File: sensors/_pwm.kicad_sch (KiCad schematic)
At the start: 21 parts, among them U2 PCA9685PW, Y2 ASE-xxxMHz

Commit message: add Vref
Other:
- title: (none) -> PilotPi: Sensors
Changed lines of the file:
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@@
 	(generator_version "10.0")
 	(paper "A4")
+	(title_block
+		(title "PilotPi: Sensors")
+		(date "15 nov 2012")
+		(rev "4")
+	)
 	(junction
 		(at 184.15 80.01)

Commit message: added JP_VOLTS, Vref select jumper; VBAT_ADC Jumper
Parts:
- C4, C5: Part (none) -> CC0402X7R50V104KN
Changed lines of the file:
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@@
 			)
 		)
-		(property "Part" ""
+		(property "Part" "CC0402X7R50V104KN"
 			(at 30.48 92.71 0)
 			(hide yes)
@@
 			)
 		)
-		(property "Part" ""
+		(property "Part" "CC0402X7R50V104KN"
 			(at 256.54 92.71 0)
 			(hide yes)

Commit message: use CLK out from CAN controller for UART (use 16 MHz instead of 14.7456MHz); minor changes
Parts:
- C4, C5: value 100nF (104) 10% 16V -> 100nF 10% 16V
- R12: value 3.3KΩ (3301) ±1% -> 3.3KΩ ±1%
- R13, R14, R15, R16, R17, R18, R19, R20, R21, R22, R23, R24, R25, R26, R27, R28: value 220Ω (2200) ±1% -> 220Ω ±1%
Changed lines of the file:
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@@
 			)
 		)
-		(property "Value" "220Ω (2200) ±1%"
+		(property "Value" "220Ω ±1%"
 			(at 129.032 96.774 90)
 			(show_name no)
@@
 			)
 		)
-		(property "Value" "220Ω (2200) ±1%"
+		(property "Value" "220Ω ±1%"
 			(at 104.902 89.154 90)
 			(show_name no)
@@
 			)
 		)
-		(property "Value" "220Ω (2200) ±1%"
+		(property "Value" "220Ω ±1%"
 			(at 104.902 78.994 90)
 			(show_name no)
@@
 			)
 		)
-		(property "Value" "220Ω (2200) ±1%"
+		(property "Value" "220Ω ±1%"
 			(at 129.032 81.534 90)
 			(show_name no)
@@
 			)
 		)
-		(property "Value" "220Ω (2200) ±1%"
+		(property "Value" "220Ω ±1%"
 			(at 104.902 73.914 90)
 			(show_name no)
@@
 			)
 		)
-		(property "Value" "220Ω (2200) ±1%"
+		(property "Value" "220Ω ±1%"
 			(at 104.902 94.234 90)
 			(show_name no)
@@
 			)
 		)
-		(property "Value" "220Ω (2200) ±1%"
+		(property "Value" "220Ω ±1%"
 			(at 129.032 112.014 90)
 			(show_name no)
@@
 			)
 		)
-		(property "Value" "220Ω (2200) ±1%"
+		(property "Value" "220Ω ±1%"
 			(at 104.902 109.474 90)
 			(show_name no)
@@
 			)
 		)
-		(property "Value" "220Ω (2200) ±1%"
+		(property "Value" "220Ω ±1%"
 			(at 104.902 99.314 90)
 			(show_name no)
@@
 			)
 		)
-		(property "Value" "220Ω (2200) ±1%"
+		(property "Value" "220Ω ±1%"
 			(at 129.032 91.694 90)
 			(show_name no)
@@
 			)
 		)
-		(property "Value" "220Ω (2200) ±1%"
+		(property "Value" "220Ω ±1%"
 			(at 129.032 106.934 90)
 			(show_name no)
@@
 			)
 		)
-		(property "Value" "220Ω (2200) ±1%"
+		(property "Value" "220Ω ±1%"
 			(at 129.032 101.854 90)
 			(show_name no)
@@
 			)
 		)
-		(property "Value" "100nF (104) 10% 16V"
+		(property "Value" "100nF 10% 16V"
 			(at 25.146 101.092 90)
 			(show_name no)
@@
 			)
 		)
-		(property "Value" "220Ω (2200) ±1%"
+		(property "Value" "220Ω ±1%"
 			(at 129.032 76.454 90)
 			(show_name no)
@@
 			)
 		)
-		(property "Value" "100nF (104) 10% 16V"
+		(property "Value" "100nF 10% 16V"
 			(at 262.89 98.806 90)
 			(show_name no)
@@
 			)
 		)
-		(property "Value" "220Ω (2200) ±1%"
+		(property "Value" "220Ω ±1%"
 			(at 104.902 104.394 90)
 			(show_name no)
@@
 			)
 		)
-		(property "Value" "220Ω (2200) ±1%"
+		(property "Value" "220Ω ±1%"
 			(at 104.902 84.074 90)
 			(show_name no)
@@
 			)
 		)
-		(property "Value" "3.3KΩ (3301) ±1%"
+		(property "Value" "3.3KΩ ±1%"
 			(at 188.468 92.964 90)
 			(show_name no)
@@
 			)
 		)
-		(property "Value" "220Ω (2200) ±1%"
+		(property "Value" "220Ω ±1%"
 			(at 129.032 86.614 90)
 			(show_name no)

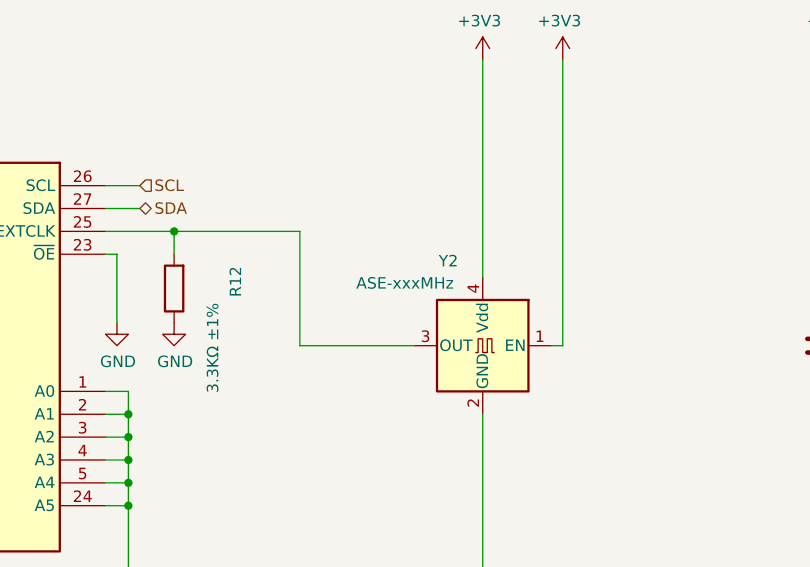
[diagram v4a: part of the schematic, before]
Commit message: use 2x8 for ADC header; added part numbers
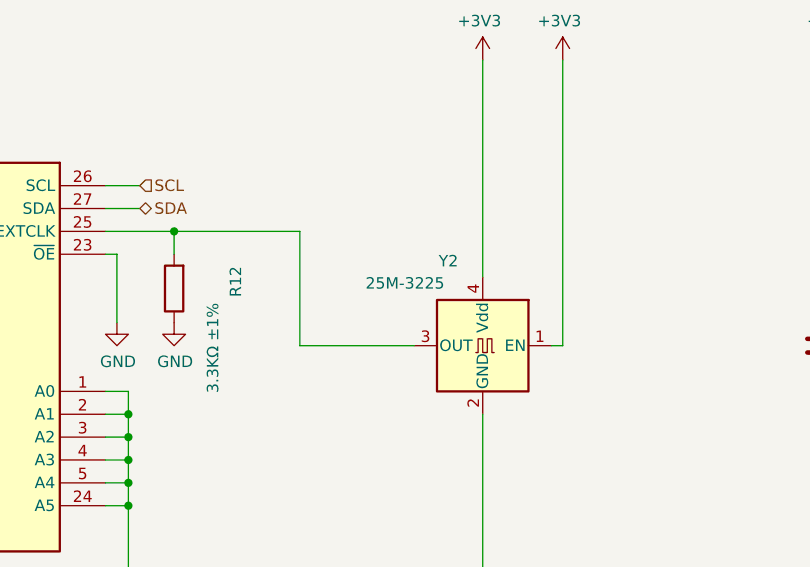
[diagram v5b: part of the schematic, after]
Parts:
- R12: Part (none) -> 0402WGF3301TCE
- R13, R14, R15, R16, R17, R18, R19, R20, R21, R22, R23, R24, R25, R26, R27, R28: Part (none) -> RC0402FR-07220RL
- U2: Part (none) -> PCA9685PW/Q900,118
- Y2: value ASE-xxxMHz -> 25M-3225; Part (none) -> Y322525MNCCZ
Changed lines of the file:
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@@
 			)
 		)
-		(property "Part" ""
+		(property "Part" "RC0402FR-07220RL"
 			(at 116.84 97.79 0)
 			(hide yes)
@@
 			)
 		)
-		(property "Part" ""
+		(property "Part" "RC0402FR-07220RL"
 			(at 92.71 90.17 0)
 			(hide yes)
@@
 			)
 		)
-		(property "Part" ""
+		(property "Part" "RC0402FR-07220RL"
 			(at 92.71 80.01 0)
 			(hide yes)
@@
 			)
 		)
-		(property "Part" ""
+		(property "Part" "RC0402FR-07220RL"
 			(at 116.84 82.55 0)
 			(hide yes)
@@
 			)
 		)
-		(property "Part" ""
+		(property "Part" "RC0402FR-07220RL"
 			(at 92.71 74.93 0)
 			(hide yes)
@@
 			)
 		)
-		(property "Part" ""
+		(property "Part" "RC0402FR-07220RL"
 			(at 92.71 95.25 0)
 			(hide yes)
@@
 			)
 		)
-		(property "Part" ""
+		(property "Part" "RC0402FR-07220RL"
 			(at 116.84 113.03 0)
 			(hide yes)
@@
 			)
 		)
-		(property "Part" ""
+		(property "Part" "RC0402FR-07220RL"
 			(at 92.71 110.49 0)
 			(hide yes)
@@
 			)
 		)
+		(property "Part" "PCA9685PW/Q900,118"
+			(at 158.75 92.71 0)
+			(hide yes)
+			(show_name no)
+			(do_not_autoplace no)
+			(effects
+				(font
+					(size 1.27 1.27)
+				)
+			)
+		)
 		(pin "10"
 		)
@@
 			)
 		)
-		(property "Part" ""
+		(property "Part" "RC0402FR-07220RL"
 			(at 92.71 100.33 0)
 			(hide yes)
@@
 			)
 		)
-		(property "Part" ""
+		(property "Part" "RC0402FR-07220RL"
 			(at 116.84 92.71 0)
 			(hide yes)
@@
 			)
 		)
-		(property "Part" ""
+		(property "Part" "RC0402FR-07220RL"
 			(at 116.84 107.95 0)
 			(hide yes)
@@
 			)
 		)
-		(property "Part" ""
+		(property "Part" "RC0402FR-07220RL"
 			(at 116.84 102.87 0)
 			(hide yes)
@@
 			)
 		)
-		(property "Part" ""
+		(property "Part" "RC0402FR-07220RL"
 			(at 116.84 77.47 0)
 			(hide yes)
@@
 			)
 		)
-		(property "Part" ""
+		(property "Part" "RC0402FR-07220RL"
 			(at 92.71 105.41 0)
 			(hide yes)
@@
 			)
 		)
-		(property "Part" ""
+		(property "Part" "RC0402FR-07220RL"
 			(at 92.71 85.09 0)
 			(hide yes)
@@
 			)
 		)
-		(property "Part" ""
+		(property "Part" "0402WGF3301TCE"
 			(at 184.15 86.36 0)
 			(hide yes)
@@
 			)
 		)
-		(property "Part" ""
+		(property "Part" "RC0402FR-07220RL"
 			(at 116.84 87.63 0)
 			(hide yes)
@@
 			)
 		)
-		(property "Value" "ASE-xxxMHz"
+		(property "Value" "25M-3225"
 			(at 209.804 85.7818 0)
 			(show_name no)
@@
 			(at 218.44 92.71 0)
 			(hide yes)
+			(show_name no)
+			(do_not_autoplace no)
+			(effects
+				(font
+					(size 1.27 1.27)
+				)
+			)
+		)
+		(property "Part" "Y322525MNCCZ"
+			(at 218.44 92.71 0)
+			(hide yes)

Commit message: replace MS561101 pressure sensor with SPL06-001
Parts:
- C4, C5: Part CC0402X7R50V104KN -> CL05B104KB54PNC
- R13, R14, R15, R16, R17, R18, R19, R20, R21, R22, R23, R24, R25, R26, R27, R28: Part RC0402FR-07220RL -> 0402WGF2200TCE
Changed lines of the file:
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@@
 			)
 		)
-		(property "Part" "RC0402FR-07220RL"
+		(property "Part" "0402WGF2200TCE"
 			(at 116.84 97.79 0)
 			(hide yes)
@@
 			)
 		)
-		(property "Part" "RC0402FR-07220RL"
+		(property "Part" "0402WGF2200TCE"
 			(at 92.71 90.17 0)
 			(hide yes)
@@
 			)
 		)
-		(property "Part" "RC0402FR-07220RL"
+		(property "Part" "0402WGF2200TCE"
 			(at 92.71 80.01 0)
 			(hide yes)
@@
 			)
 		)
-		(property "Part" "RC0402FR-07220RL"
+		(property "Part" "0402WGF2200TCE"
 			(at 116.84 82.55 0)
 			(hide yes)
@@
 			)
 		)
-		(property "Part" "RC0402FR-07220RL"
+		(property "Part" "0402WGF2200TCE"
 			(at 92.71 74.93 0)
 			(hide yes)
@@
 			)
 		)
-		(property "Part" "RC0402FR-07220RL"
+		(property "Part" "0402WGF2200TCE"
 			(at 92.71 95.25 0)
 			(hide yes)
@@
 			)
 		)
-		(property "Part" "RC0402FR-07220RL"
+		(property "Part" "0402WGF2200TCE"
 			(at 116.84 113.03 0)
 			(hide yes)
@@
 			)
 		)
-		(property "Part" "RC0402FR-07220RL"
+		(property "Part" "0402WGF2200TCE"
 			(at 92.71 110.49 0)
 			(hide yes)
@@
 			)
 		)
-		(property "Part" "RC0402FR-07220RL"
+		(property "Part" "0402WGF2200TCE"
 			(at 92.71 100.33 0)
 			(hide yes)
@@
 			)
 		)
-		(property "Part" "RC0402FR-07220RL"
+		(property "Part" "0402WGF2200TCE"
 			(at 116.84 92.71 0)
 			(hide yes)
@@
 			)
 		)
-		(property "Part" "RC0402FR-07220RL"
+		(property "Part" "0402WGF2200TCE"
 			(at 116.84 107.95 0)
 			(hide yes)
@@
 			)
 		)
-		(property "Part" "RC0402FR-07220RL"
+		(property "Part" "0402WGF2200TCE"
 			(at 116.84 102.87 0)
 			(hide yes)
@@
 			)
 		)
-		(property "Part" "CC0402X7R50V104KN"
+		(property "Part" "CL05B104KB54PNC"
 			(at 30.48 92.71 0)
 			(hide yes)
@@
 			)
 		)
-		(property "Part" "RC0402FR-07220RL"
+		(property "Part" "0402WGF2200TCE"
 			(at 116.84 77.47 0)
 			(hide yes)
@@
 			)
 		)
-		(property "Part" "CC0402X7R50V104KN"
+		(property "Part" "CL05B104KB54PNC"
 			(at 256.54 92.71 0)
 			(hide yes)
@@
 			)
 		)
-		(property "Part" "RC0402FR-07220RL"
+		(property "Part" "0402WGF2200TCE"
 			(at 92.71 105.41 0)
 			(hide yes)
@@
 			)
 		)
-		(property "Part" "RC0402FR-07220RL"
+		(property "Part" "0402WGF2200TCE"
 			(at 92.71 85.09 0)
 			(hide yes)
@@
 			)
 		)
-		(property "Part" "RC0402FR-07220RL"
+		(property "Part" "0402WGF2200TCE"
 			(at 116.84 87.63 0)
 			(hide yes)

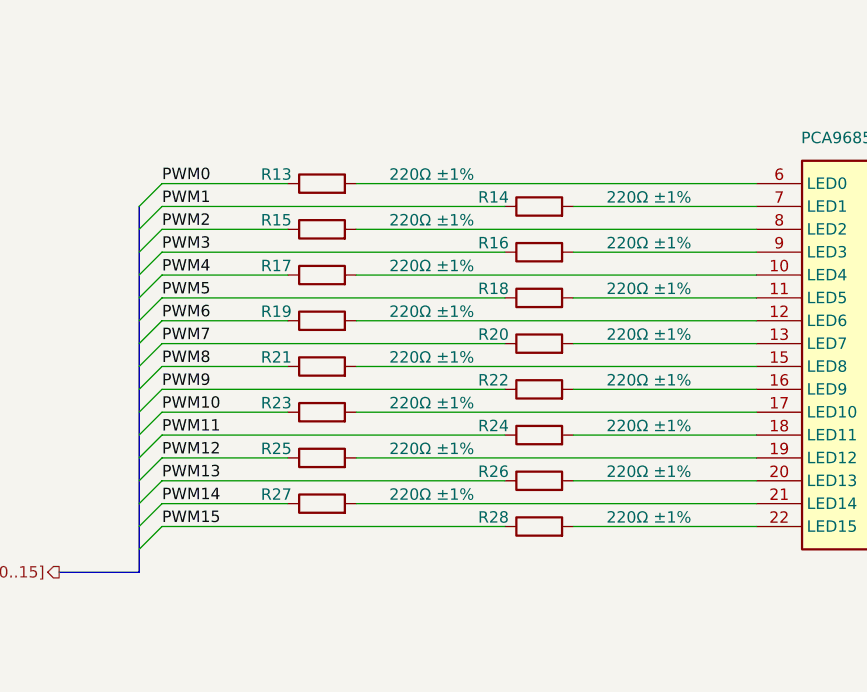
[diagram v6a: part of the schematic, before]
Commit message: move SP3485 to sensors board and connect to UART port A
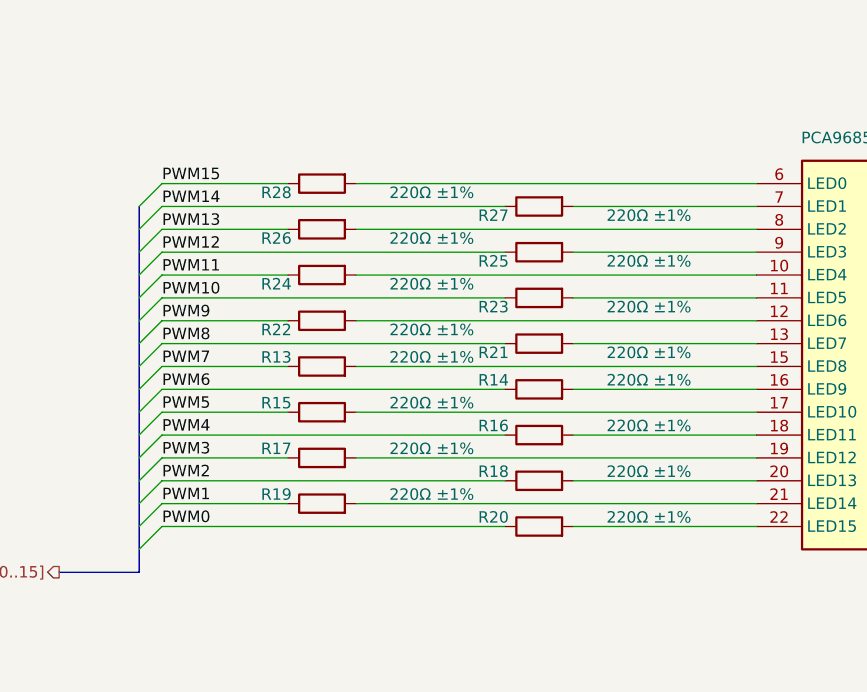
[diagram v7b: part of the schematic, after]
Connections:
- net PWM0: now also R20.1; no longer R13.1
- net PWM1: now also R19.1; no longer R14.1
- net PWM2: now also R18.1; no longer R15.1
- net PWM3: now also R17.1; no longer R16.1
- net PWM4: now also R16.1; no longer R17.1
- net PWM5: now also R15.1; no longer R18.1
- net PWM6: now also R14.1; no longer R19.1
- net PWM7: now also R13.1; no longer R20.1
- net at R22.2: now also U2.12 (LED6); no longer U2.16 (LED9)
- net at R19.2: now also U2.21 (LED14); no longer U2.12 (LED6)
- net at R15.2: now also U2.17 (LED10); no longer U2.8 (LED2)
- net at R16.2: now also U2.18 (LED11); no longer U2.9 (LED3)
- net at R13.2: now also U2.15 (LED8); no longer U2.6 (LED0)
- net at R21.2: now also U2.13 (LED7); no longer U2.15 (LED8)
- net at R28.2: now also U2.6 (LED0); no longer U2.22 (LED15)
- net at R27.2: now also U2.7 (LED1); no longer U2.21 (LED14)
- net at U2.10 (LED4): now also R24.2; no longer R17.2
- net at U2.11 (LED5): now also R23.2; no longer R18.2
- net at R20.2: now also U2.22 (LED15); no longer U2.13 (LED7)
- net at U2.19 (LED12): now also R17.2; no longer R25.2
- net at U2.20 (LED13): now also R18.2; no longer R26.2
- net at R14.2: now also U2.16 (LED9); no longer U2.7 (LED1)
- new net: R26.2, U2.8 (LED2)
- new net: R25.2, U2.9 (LED3)
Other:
- moved on the sheet: R13, R14, R15, R16, R17, R18, R19, R20, R21, R22, R23, R24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

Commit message: use series resistor for external clk; add 1uF caps
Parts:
- added C20: 1uF (105) 10% 50V, Capacitor_SMD:C_0603_1608Metric, symbol Device:C
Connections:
- net +5V: now also C20.1
- net GND: now also C20.2
